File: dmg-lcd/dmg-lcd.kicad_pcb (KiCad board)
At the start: 2 copper layers, 81 x 79 mm, 4 parts

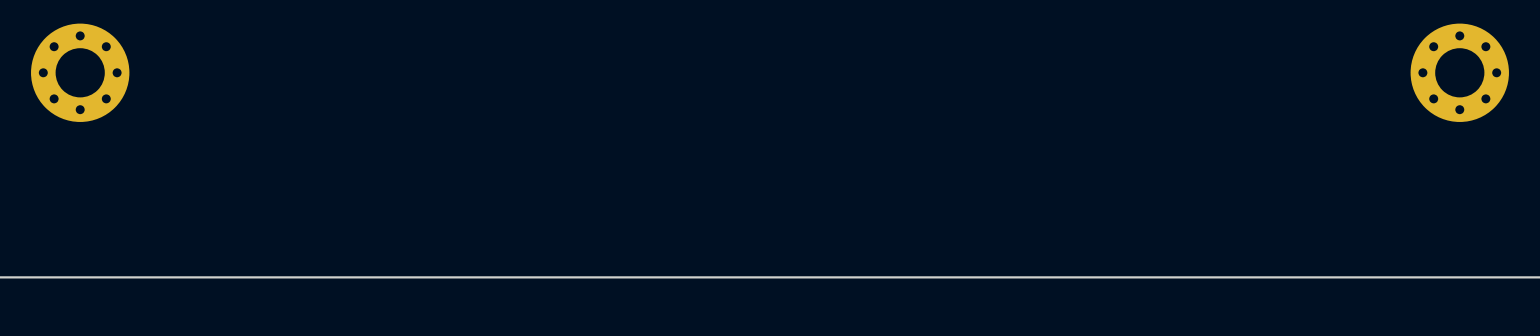
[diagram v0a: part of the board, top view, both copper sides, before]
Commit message: feat: Add battery terminals
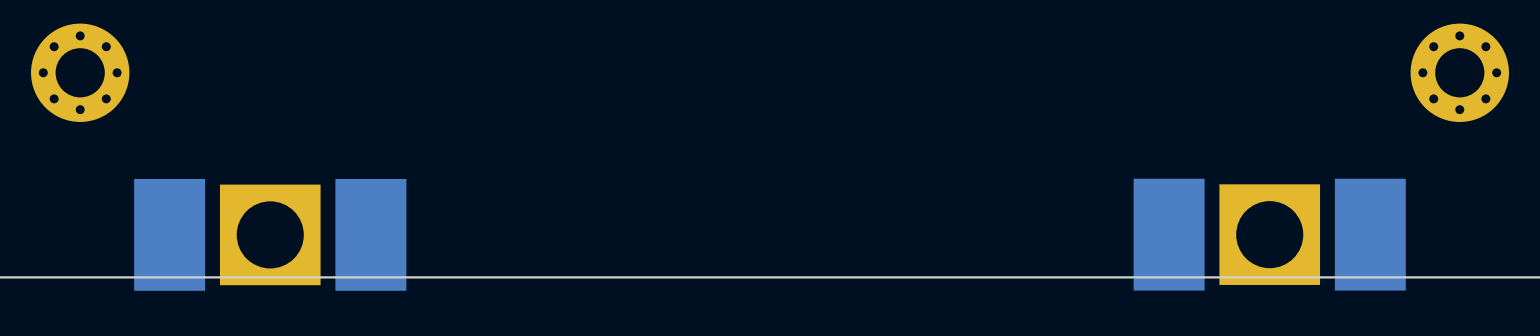
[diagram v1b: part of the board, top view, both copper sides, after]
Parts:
- added J1: Conn_01x01_Pin, dmg-lcd:Battery_Terminal, B.Cu at (162.9, 127.1)
- added J2: Conn_01x01_Pin, dmg-lcd:Battery_Terminal, B.Cu at (118.2, 127.1)
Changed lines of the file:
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@@
   )
   (net 0 "")
+  (net 1 "unconnected-(J1-Pin_1-Pad1)")
+  (net 2 "unconnected-(J2-Pin_1-Pad1)")
   (footprint "MountingHole:MountingHole_2.2mm_M2_Pad_Via" (layer "F.Cu")
     (at 171.375 119.85)
@@
     (pad "1" thru_hole circle (at 1.875 0) (size 0.8 0.8) (drill 0.5) (layers "*.Cu" "*.Mask"))
   )
+  (footprint "dmg-lcd:Battery_Terminal" (layer "B.Cu")
+    (at 162.875 127.089 180)
+    (property "Sheetfile" "dmg-lcd.kicad_sch")
+    (property "Sheetname" "")
+    (property "ki_description" "Generic connector, single row, 01x01, script generated")
+    (property "ki_keywords" "connector")
+    (fp_text reference "J1" (at 0 3.81 unlocked) (layer "B.SilkS") hide
+        (effects (font (size 1 1) (thickness 0.1)) (justify mirror))
+    )
+    (fp_text value "Conn_01x01_Pin" (at 0 -3.81 unlocked) (layer "B.Fab") hide
+        (effects (font (size 1 1) (thickness 0.15)) (justify mirror))
+    )
+    (pad "1" smd rect (at -4.5 0 180) (size 3.175 5) (layers "B.Cu" "B.Paste" "B.Mask")
+      (net 1 "unconnected-(J1-Pin_1-Pad1)") (pinfunction "Pin_1") (pintype "passive"))
+    (pad "1" thru_hole rect (at 0 0 180) (size 4.5 4.5) (drill 3) (layers "*.Cu" "*.Mask")
+      (net 1 "unconnected-(J1-Pin_1-Pad1)") (pinfunction "Pin_1") (pintype "passive"))
+    (pad "1" smd rect (at 4.5 0 180) (size 3.175 5) (layers "B.Cu" "B.Paste" "B.Mask")
+      (net 1 "unconnected-(J1-Pin_1-Pad1)") (pinfunction "Pin_1") (pintype "passive"))
+  )
+  (footprint "dmg-lcd:Battery_Terminal" (layer "B.Cu")
+    (at 118.175 127.1 180)
+    (property "Sheetfile" "dmg-lcd.kicad_sch")
+    (property "Sheetname" "")
+    (property "ki_description" "Generic connector, single row, 01x01, script generated")
+    (property "ki_keywords" "connector")
+    (fp_text reference "J2" (at 0 3.81 unlocked) (layer "B.SilkS") hide
+        (effects (font (size 1 1) (thickness 0.1)) (justify mirror))
+    )
+    (fp_text value "Conn_01x01_Pin" (at 0 -3.81 unlocked) (layer "B.Fab") hide
+        (effects (font (size 1 1) (thickness 0.15)) (justify mirror))
+    )
+    (pad "1" smd rect (at -4.5 0 180) (size 3.175 5) (layers "B.Cu" "B.Paste" "B.Mask")
+      (net 2 "unconnected-(J2-Pin_1-Pad1)") (pinfunction "Pin_1") (pintype "passive"))
+    (pad "1" thru_hole rect (at 0 0 180) (size 4.5 4.5) (drill 3) (layers "*.Cu" "*.Mask")
+      (net 2 "unconnected-(J2-Pin_1-Pad1)") (pinfunction "Pin_1") (pintype "passive"))
+    (pad "1" smd rect (at 4.5 0 180) (size 3.175 5) (layers "B.Cu" "B.Paste" "B.Mask")
+      (net 2 "unconnected-(J2-Pin_1-Pad1)") (pinfunction "Pin_1") (pintype "passive"))
+  )
   (gr_line (start 100 50) (end 181 50)

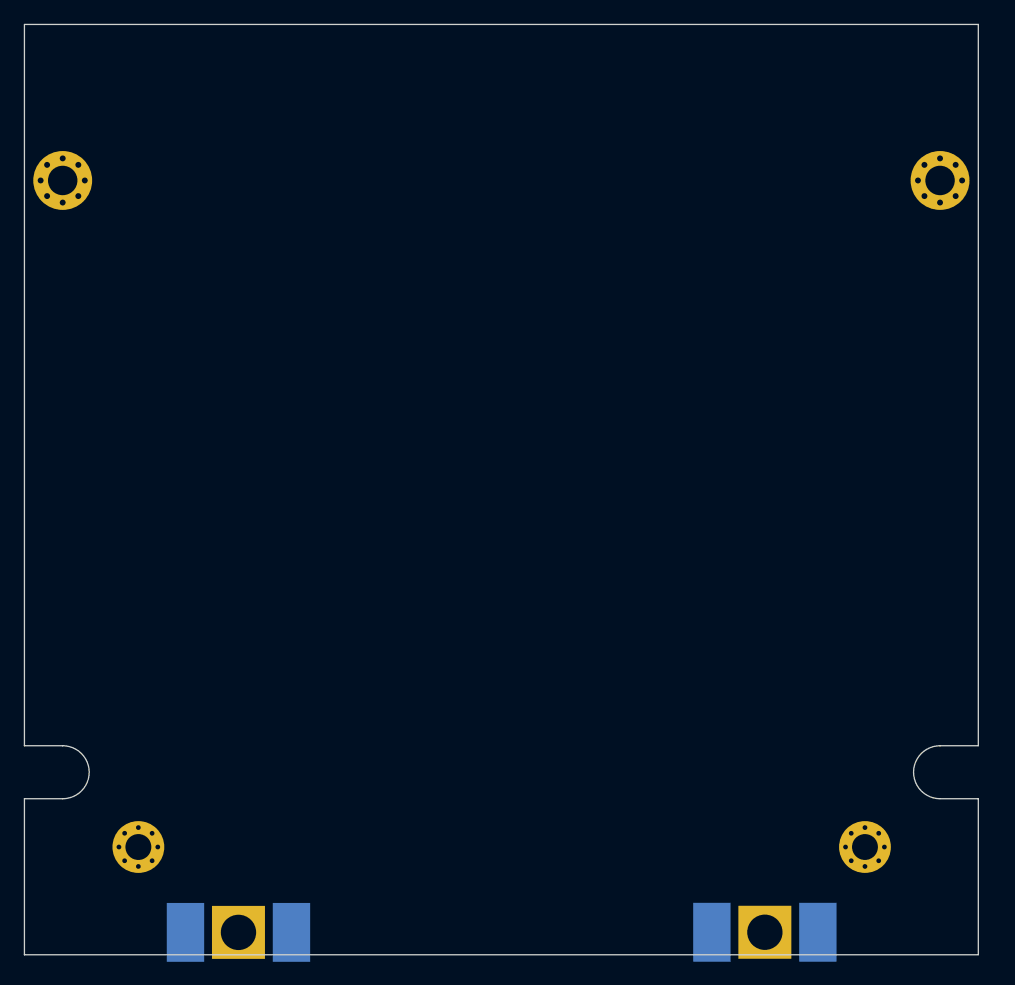
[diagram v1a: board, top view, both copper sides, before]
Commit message: feat: Add potentiometers and volumn switch
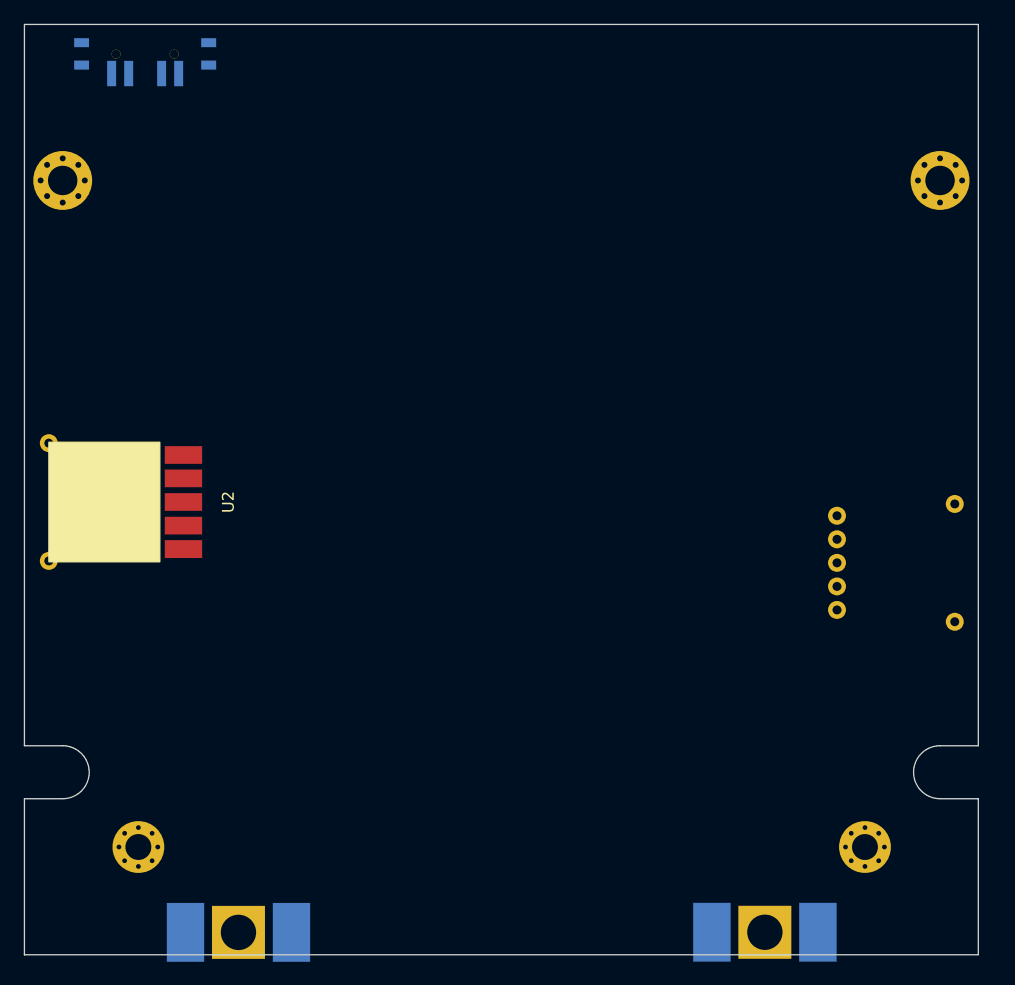
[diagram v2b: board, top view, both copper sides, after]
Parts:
- added SW1: Power Switch, dmg-lcd:Power_Switch, B.Cu at (110.2, 51.2)
- added U1: ~, dmg-lcd:Volume_Potentiometer, B.Cu at (169.0, 95.7)
- added U2: ~, dmg-lcd:Contrast_Potentiometer, F.Cu at (113.5, 90.6)
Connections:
- J1 pad 1: unconnected-(J1-Pin_1-Pad1) -> -BATT
- J2 pad 1: unconnected-(J2-Pin_1-Pad1) -> +BATT
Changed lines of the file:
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@@
   )
   (net 0 "")
-  (net 1 "unconnected-(J1-Pin_1-Pad1)")
-  (net 2 "unconnected-(J2-Pin_1-Pad1)")
+  (net 1 "-BATT")
+  (net 2 "+BATT")
+  (net 3 "unconnected-(U1-Pad1)")
+  (net 4 "unconnected-(U1-Pad2)")
+  (net 5 "unconnected-(U1-Pad3)")
+  (net 6 "unconnected-(U1-Pad4)")
+  (net 7 "unconnected-(U1-Pad5)")
+  (net 8 "unconnected-(U2-Pad1)")
+  (net 9 "unconnected-(U2-Pad2)")
+  (net 10 "unconnected-(U2-Pad3)")
+  (net 11 "unconnected-(U2-Pad4)")
+  (net 12 "unconnected-(U2-Pad5)")
+  (net 13 "unconnected-(SW1-Pad1)")
+  (net 14 "unconnected-(SW1-Pad2)")
+  (net 15 "unconnected-(SW1-Pad3)")
+  (net 16 "unconnected-(SW1-Pad4)")
   (footprint "MountingHole:MountingHole_2.2mm_M2_Pad_Via" (layer "F.Cu")
     (at 171.375 119.85)
@@
     (pad "1" thru_hole circle (at 1.65 0) (size 0.7 0.7) (drill 0.4) (layers "*.Cu" "*.Mask"))
   )
+  (footprint "dmg-lcd:Contrast_Potentiometer" (layer "F.Cu")
+    (at 113.5 90.555 90)
+    (property "Sheetfile" "dmg-lcd.kicad_sch")
+    (property "Sheetname" "")
+    (attr smd)
+    (fp_text reference "U2" (at 0 3.81 90 unlocked) (layer "F.SilkS")
+        (effects (font (size 1 1) (thickness 0.1)))
+    )
+    (fp_text value "~" (at 0 11.43 90 unlocked) (layer "F.Fab") hide
+        (effects (font (size 1 1) (thickness 0.15)))
+    )
+    (fp_rect (start -5.08 -11.43) (end 5.08 -2)
+      (stroke (width 0.1) (type solid)) (fill solid) (layer "F.SilkS"))
+    (fp_circle (center 0 -9) (end 7.15 -9)
+      (stroke (width 0.05) (type default)) (fill none) (layer "F.CrtYd"))
+    (pad "1" smd rect (at -4 0 90) (size 1.5 3.175) (layers "F.Cu" "F.Paste" "F.Mask")
+      (net 8 "unconnected-(U2-Pad1)") (pintype "passive") (thermal_bridge_angle 45))
+    (pad "2" smd rect (at -2 0 90) (size 1.5 3.175) (layers "F.Cu" "F.Paste" "F.Mask")
+      (net 9 "unconnected-(U2-Pad2)") (pintype "passive") (thermal_bridge_angle 45))
+    (pad "3" smd rect (at 0 0 90) (size 1.5 3.175) (layers "F.Cu" "F.Paste" "F.Mask")
+      (net 10 "unconnected-(U2-Pad3)") (pintype "passive") (thermal_bridge_angle 45))
+    (pad "4" smd rect (at 2 0 90) (size 1.5 3.175) (layers "F.Cu" "F.Paste" "F.Mask")
+      (net 11 "unconnected-(U2-Pad4)") (pintype "passive") (thermal_bridge_angle 45))
+    (pad "5" smd rect (at 4 0 90) (size 1.5 3.175) (layers "F.Cu" "F.Paste" "F.Mask")
+      (net 12 "unconnected-(U2-Pad5)") (pintype "passive") (thermal_bridge_angle 45))
+    (pad "6" thru_hole circle (at -5 -11.43 90) (size 1.524 1.524) (drill 0.762) (layers "*.Cu" "*.Mask"))
+    (pad "6" thru_hole circle (at 5 -11.43 90) (size 1.524 1.524) (drill 0.762) (layers "*.Cu" "*.Mask"))
+  )
   (footprint "MountingHole:MountingHole_2.5mm_Pad_Via" (layer "F.Cu")
     (at 177.75 63.25)
@@
     (pad "1" thru_hole circle (at 1.875 0) (size 0.8 0.8) (drill 0.5) (layers "*.Cu" "*.Mask"))
   )
+  (footprint "dmg-lcd:Power_Switch" (layer "B.Cu")
+    (at 110.25 51.25 180)
+    (property "Sheetfile" "dmg-lcd.kicad_sch")
+    (property "Sheetname" "")
+    (property "ki_description" "Double Pole Single Throw (DPST) Switch")
+    (property "ki_keywords" "switch dual double-pole single-throw OFF-ON")
+    (attr smd)
+    (fp_text reference "SW1" (at 0 2.54 unlocked) (layer "B.SilkS") hide
+        (effects (font (size 1 1) (thickness 0.1)) (justify mirror))
+    )
+    (fp_text value "Power Switch" (at 0 -6.35 unlocked) (layer "B.Fab") hide
+        (effects (font (size 1 1) (thickness 0.15)) (justify mirror))
+    )
+    (fp_rect (start -4.826 0) (end 4.826 -2.54)
+      (stroke (width 0.1) (type default)) (fill none) (layer "Dwgs.User"))
+    (pad "" smd rect (at -5.4 -2.2 180) (size 1.27 0.762) (layers "B.Cu" "B.Paste" "B.Mask")
+      (thermal_bridge_angle 45))
+    (pad "" smd rect (at -5.4 -0.3 180) (size 1.27 0.762) (layers "B.Cu" "B.Paste" "B.Mask")
+      (thermal_bridge_angle 45))
+    (pad "" thru_hole circle (at -2.4638 -1.27 180) (size 0.762 0.762) (drill 0.762) (layers "*.Cu" "*.Mask"))
+    (pad "" thru_hole circle (at 2.4638 -1.27 180) (size 0.762 0.762) (drill 0.762) (layers "*.Cu" "*.Mask"))
+    (pad "" smd rect (at 5.4 -2.2 180) (size 1.27 0.762) (layers "B.Cu" "B.Paste" "B.Mask")
+      (thermal_bridge_angle 45))
+    (pad "" smd rect (at 5.4 -0.3 180) (size 1.27 0.762) (layers "B.Cu" "B.Paste" "B.Mask")
+      (thermal_bridge_angle 45))
+    (pad "1" smd rect (at -2.8448 -2.921 90) (size 2.159 0.762) (layers "B.Cu" "B.Paste" "B.Mask")
+      (net 13 "unconnected-(SW1-Pad1)") (pinfunction "1") (pintype "passive") (thermal_bridge_angle 45))
+    (pad "2" smd rect (at -1.397 -2.921 90) (size 2.159 0.762) (layers "B.Cu" "B.Paste" "B.Mask")
+      (net 14 "unconnected-(SW1-Pad2)") (pinfunction "2") (pintype "passive") (thermal_bridge_angle 45))
+    (pad "3" smd rect (at 1.397 -2.921 90) (size 2.159 0.762) (layers "B.Cu" "B.Paste" "B.Mask")
+      (net 15 "unconnected-(SW1-Pad3)") (pinfunction "3") (pintype "passive") (thermal_bridge_angle 45))
+    (pad "4" smd rect (at 2.8448 -2.921 90) (size 2.159 0.762) (layers "B.Cu" "B.Paste" "B.Mask")
+      (net 16 "unconnected-(SW1-Pad4)") (pinfunction "4") (pintype "passive") (thermal_bridge_angle 45))
+  )
   (footprint "dmg-lcd:Battery_Terminal" (layer "B.Cu")
     (at 162.875 127.089 180)
@@
     )
     (pad "1" smd rect (at -4.5 0 180) (size 3.175 5) (layers "B.Cu" "B.Paste" "B.Mask")
-      (net 1 "unconnected-(J1-Pin_1-Pad1)") (pinfunction "Pin_1") (pintype "passive"))
+      (net 1 "-BATT") (pinfunction "Pin_1") (pintype "passive"))
     (pad "1" thru_hole rect (at 0 0 180) (size 4.5 4.5) (drill 3) (layers "*.Cu" "*.Mask")
-      (net 1 "unconnected-(J1-Pin_1-Pad1)") (pinfunction "Pin_1") (pintype "passive"))
+      (net 1 "-BATT") (pinfunction "Pin_1") (pintype "passive"))
     (pad "1" smd rect (at 4.5 0 180) (size 3.175 5) (layers "B.Cu" "B.Paste" "B.Mask")
-      (net 1 "unconnected-(J1-Pin_1-Pad1)") (pinfunction "Pin_1") (pintype "passive"))
+      (net 1 "-BATT") (pinfunction "Pin_1") (pintype "passive"))
   )
   (footprint "dmg-lcd:Battery_Terminal" (layer "B.Cu")
@@
     )
     (pad "1" smd rect (at -4.5 0 180) (size 3.175 5) (layers "B.Cu" "B.Paste" "B.Mask")
-      (net 2 "unconnected-(J2-Pin_1-Pad1)") (pinfunction "Pin_1") (pintype "passive"))
+      (net 2 "+BATT") (pinfunction "Pin_1") (pintype "passive"))
     (pad "1" thru_hole rect (at 0 0 180) (size 4.5 4.5) (drill 3) (layers "*.Cu" "*.Mask")
-      (net 2 "unconnected-(J2-Pin_1-Pad1)") (pinfunction "Pin_1") (pintype "passive"))
+      (net 2 "+BATT") (pinfunction "Pin_1") (pintype "passive"))
     (pad "1" smd rect (at 4.5 0 180) (size 3.175 5) (layers "B.Cu" "B.Paste" "B.Mask")
-      (net 2 "unconnected-(J2-Pin_1-Pad1)") (pinfunction "Pin_1") (pintype "passive"))
+      (net 2 "+BATT") (pinfunction "Pin_1") (pintype "passive"))
+  )
+  (footprint "dmg-lcd:Volume_Potentiometer" (layer "B.Cu")
+    (at 169 95.72 90)
+    (property "Sheetfile" "dmg-lcd.kicad_sch")
+    (property "Sheetname" "")
+    (attr through_hole)
+    (fp_text reference "U1" (at 0 11.43 270 unlocked) (layer "B.SilkS") hide
+        (effects (font (size 1 1) (thickness 0.1)) (justify mirror))
+    )
+    (fp_text value "~" (at 0 -6.12 270 unlocked) (layer "B.Fab") hide
+        (effects (font (size 1 1) (thickness 0.15)) (justify mirror))
+    )
+    (fp_rect (start -5.08 10.16) (end 5.08 0)
+      (stroke (width 0.1) (type solid)) (fill solid) (layer "B.SilkS"))
+    (fp_circle (center 0 7.25) (end 8 7.25)
+      (stroke (width 0.05) (type default)) (fill none) (layer "B.CrtYd"))
+    (pad "1" thru_hole circle (at -4 0 90) (size 1.524 1.524) (drill 0.762) (layers "*.Cu" "*.Mask")
+      (net 3 "unconnected-(U1-Pad1)") (pintype "passive"))
+    (pad "2" thru_hole circle (at -2 0 90) (size 1.524 1.524) (drill 0.762) (layers "*.Cu" "*.Mask")
+      (net 4 "unconnected-(U1-Pad2)") (pintype "passive"))
+    (pad "3" thru_hole circle (at 0 0 90) (size 1.524 1.524) (drill 0.762) (layers "*.Cu" "*.Mask")
+      (net 5 "unconnected-(U1-Pad3)") (pintype "passive"))
+    (pad "4" thru_hole circle (at 2 0 90) (size 1.524 1.524) (drill 0.762) (layers "*.Cu" "*.Mask")
+      (net 6 "unconnected-(U1-Pad4)") (pintype "passive"))
+    (pad "5" thru_hole circle (at 4 0 90) (size 1.524 1.524) (drill 0.762) (layers "*.Cu" "*.Mask")
+      (net 7 "unconnected-(U1-Pad5)") (pintype "passive"))
+    (pad "6" thru_hole circle (at -5 10 90) (size 1.524 1.524) (drill 0.762) (layers "*.Cu" "*.Mask"))
+    (pad "6" thru_hole circle (at 5 10 90) (size 1.524 1.524) (drill 0.762) (layers "*.Cu" "*.Mask"))
   )
   (gr_line (start 100 50) (end 181 50)

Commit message: feat: V1.0 of the board
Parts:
- added C1: 330nF, Capacitor_SMD:C_0603_1608Metric, B.Cu at (130.8, 70.0)
- added C2: 200nF, Capacitor_SMD:C_0603_1608Metric, B.Cu at (133.8, 70.0)
- added C3: 2.2uF, Capacitor_SMD:C_0603_1608Metric, B.Cu at (139.8, 70.0)
- added C4: 2.2uF, Capacitor_SMD:C_0603_1608Metric, B.Cu at (136.8, 70.0)
- added G***: LOGO, LOGO, F.Cu at (141.5, 100.5)
- added G***: LOGO, LOGO, B.Cu at (164.5, 55.5)
- added G***: LOGO, LOGO, B.Cu at (140.0, 101.5)
- added J10: Conn_01x01, Connector_PinHeader_2.54mm:PinHeader_1x01_P2.54mm_Vertical, F.Cu at (118.0, 120.8)
- added J3: LCD Connector, Connector_FFC-FPC:TE_3-1734839-0_1x30-1MP_P0.5mm_Horizontal, B.Cu at (140.5, 64.5)
- added J4: LCD Dev Header, Connector_PinHeader_2.54mm:PinHeader_1x15_P2.54mm_Vertical, F.Cu at (122.1, 75.5)
- added J5: Conn_01x02, Connector_PinHeader_2.54mm:PinHeader_1x02_P2.54mm_Vertical, F.Cu at (175.8, 73.5)
- added J6: Conn_01x05, Connector_PinHeader_2.54mm:PinHeader_1x05_P2.54mm_Vertical, F.Cu at (166.0, 90.6)
- added J7: Conn_01x05, Connector_PinHeader_2.54mm:PinHeader_1x05_P2.54mm_Vertical, F.Cu at (118.0, 85.4)
- added J8: Conn_01x02, Connector_PinHeader_2.54mm:PinHeader_1x02_P2.54mm_Vertical, F.Cu at (108.0, 58.0)
- added J9: Conn_01x02, Connector_PinHeader_2.54mm:PinHeader_1x02_P2.54mm_Vertical, F.Cu at (112.5, 58.0)
- added R1: 10M, Resistor_SMD:R_0603_1608Metric, B.Cu at (130.8, 71.5)
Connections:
- J1 pad 1: -BATT -> VSS
- SW1 pad 1: unconnected-(SW1-Pad1) -> Net-(J9-Pin_2)
- SW1 pad 2: unconnected-(SW1-Pad2) -> Net-(J9-Pin_1)
- SW1 pad 3: unconnected-(SW1-Pad3) -> Net-(J8-Pin_1)
- SW1 pad 4: unconnected-(SW1-Pad4) -> Net-(J8-Pin_2)
- U1 pad 1: unconnected-(U1-Pad1) -> Net-(J6-Pin_5)
- U1 pad 2: unconnected-(U1-Pad2) -> Net-(J6-Pin_3)
- U1 pad 3: unconnected-(U1-Pad3) -> Net-(J6-Pin_4)
- U1 pad 4: unconnected-(U1-Pad4) -> Net-(J6-Pin_1)
- U1 pad 5: unconnected-(U1-Pad5) -> Net-(J6-Pin_2)
- U2 pad 1: unconnected-(U2-Pad1) -> Net-(J7-Pin_5)
- U2 pad 2: unconnected-(U2-Pad2) -> Net-(J7-Pin_3)
- U2 pad 3: unconnected-(U2-Pad3) -> Net-(J7-Pin_4)
- U2 pad 4: unconnected-(U2-Pad4) -> Net-(J7-Pin_1)
- U2 pad 5: unconnected-(U2-Pad5) -> Net-(J7-Pin_2)
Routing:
- net BM1: track 0.00 -> 27.6 mm
- net BM0: track 0.00 -> 24.0 mm
- net CS0: track 0.00 -> 22.2 mm
- net CD: track 0.00 -> 20.4 mm
- net D7: track 0.00 -> 19.0 mm
- net RD(E): track 0.00 -> 18.3 mm
- net D6: track 0.00 -> 16.8 mm
- net WR: track 0.00 -> 16.4 mm
- net +BATT: track 0.00 -> 15.4 mm
- net RST: track 0.00 -> 14.6 mm, vias 0 -> 1
- net D5: track 0.00 -> 14.1 mm
- net VSS: track 0.00 -> 13.6 mm, vias 0 -> 2
- net D4: track 0.00 -> 11.8 mm
- net D0: track 0.00 -> 11.7 mm
- net D1: track 0.00 -> 10.5 mm
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- added copper zone on F.Cu, net VDD
- added copper zone on B.Cu, net VSS
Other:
- board text added: "0"
- board text added: "1"
- board text added: "2"
- board text added: "3"
- board text added: "3.3V"
- board text added: "4"
- board text added: "5"
- board text added: "6"
- board text added: "7"
- board text added: "BM0"
- board text added: "BM1"
- board text added: "Batt+"
- board text added: "Battery"
- board text added: "Broderick Carlin"
- board text added: "CD"
- board text added: "COM"
- board text added: "CS"
- board text added: "Contrast"
- board text added: "Digital I/O"
- board text added: "GND"
- board text added: "LCD Circuit"
- board text added: "Power Input"
- board text added: "Power Switch"
- board text added: "R0"
- board text added: "R1"
- board text added: "RD"
- board text added: "RST"
- board text added: "V1.0"
- board text added: "Volume"
- board text added: "W/R"
- board text added: "Wiper0"
- board text added: "Wiper1"
